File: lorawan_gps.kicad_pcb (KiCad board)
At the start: 2 copper layers, 75 x 20 mm, 59 parts, among them IC1 TPS61201, P1 BL_PAD, P10 CONN_01X01, P11 CONN_01X04, P2 SWD_DAT, P3 SWD_CLK, P4 SWD_3V3, P5 SWD_GND, P6 SWD_RST, P7 CONN_01X01, P8 CONN_01X01, P9 CONN_01X01, SW1 SW_PUSH, SW2 SW_PUSH, U1 SHT21, U2 MPU-9250, U3 RFM9xW, U4 SAMD21E17A, U5 MAX-M8, Y1 32.768kHz

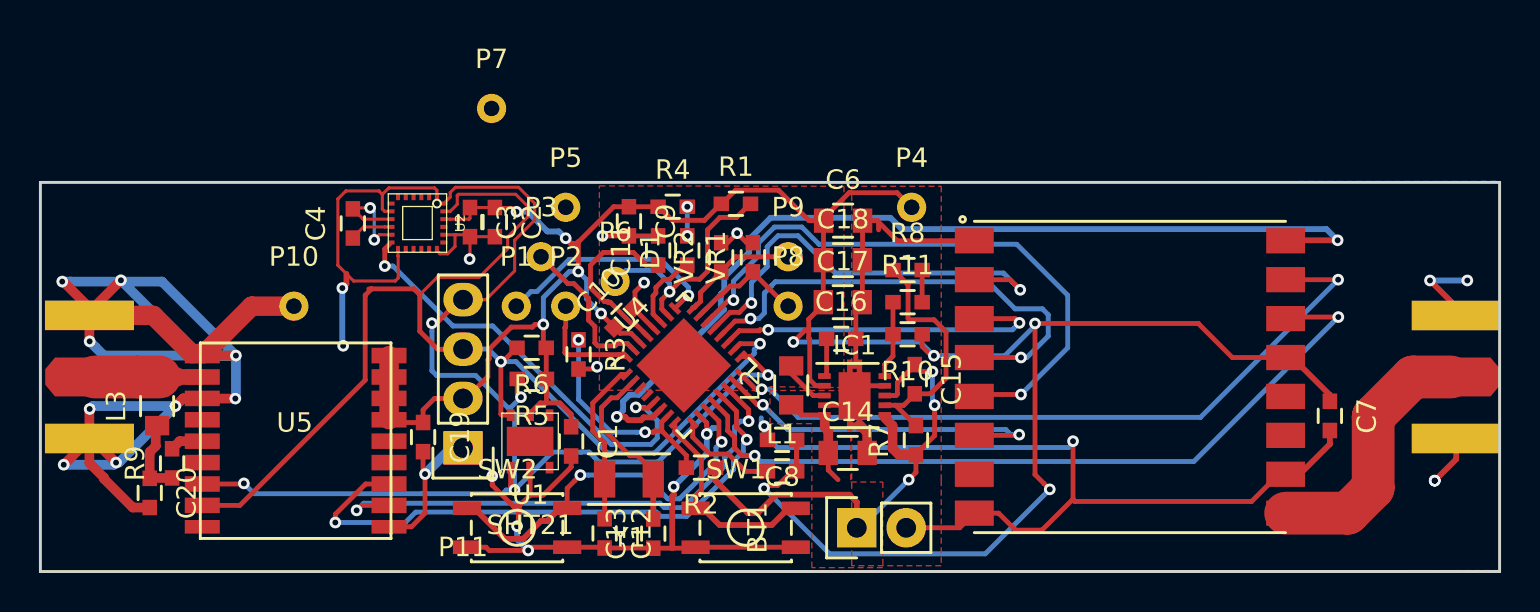
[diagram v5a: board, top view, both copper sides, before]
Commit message: moved battery input and fixed dodgy ground plane
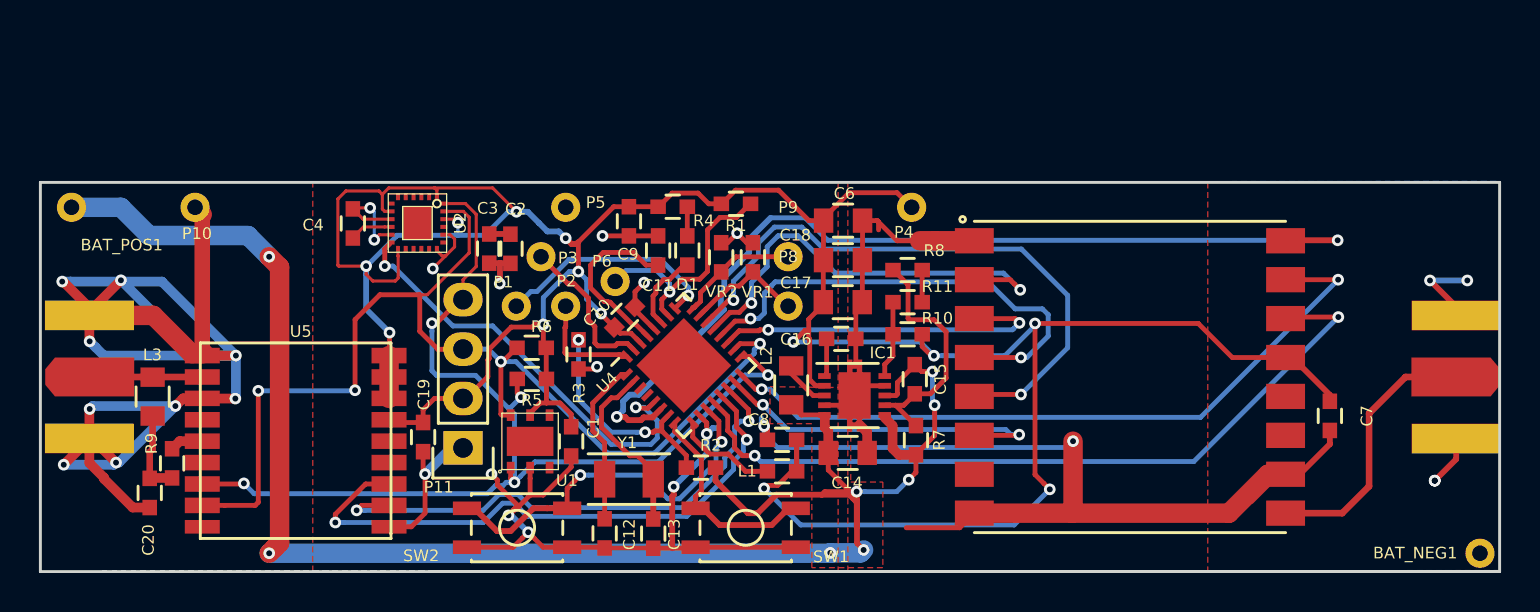
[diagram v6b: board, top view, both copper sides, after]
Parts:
- removed BT1: Battery, Pin_Headers:Pin_Header_Straight_1x02
- removed P7: CONN_01X01, Measurement_Points:Measurement_Point_Round-TH_Small
- added BAT_NEG1: CONN_01X01, Measurement_Points:Measurement_Point_Round-TH_Small, F.Cu at (174.0, 99.1)
- added BAT_POS1: CONN_01X01, Measurement_Points:Measurement_Point_Round-TH_Small, F.Cu at (101.6, 81.3)
- moved P10 7.18 mm to (108.0, 81.3)
- moved C3 1.68 mm to (123.1, 83.4)
- moved C2 1.59 mm to (124.2, 83.4)
- moved L3 0.54 mm to (105.8, 91.0)
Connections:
- U1 pad 3: Net-(U1-Pad3) -> (no net)
- U1 pad 4: Net-(U1-Pad4) -> (no net)
- U2 pad 14: Net-(U2-Pad14) -> (no net)
- U2 pad 15: Net-(U2-Pad15) -> (no net)
- U2 pad 16: Net-(U2-Pad16) -> (no net)
- U2 pad 17: Net-(U2-Pad17) -> (no net)
- U2 pad 19: Net-(U2-Pad19) -> (no net)
- U2 pad 2: Net-(U2-Pad2) -> (no net)
- U2 pad 21: Net-(U2-Pad21) -> (no net)
- U2 pad 3: Net-(U2-Pad3) -> (no net)
- U2 pad 4: Net-(U2-Pad4) -> (no net)
- U2 pad 5: Net-(U2-Pad5) -> (no net)
- U2 pad 6: Net-(U2-Pad6) -> (no net)
- U2 pad 7: Net-(U2-Pad7) -> (no net)
- U3 pad 11: Net-(U3-Pad11) -> (no net)
- U3 pad 12: Net-(U3-Pad12) -> (no net)
- U3 pad 7: Net-(U3-Pad7) -> (no net)
- U4 pad 3: Net-(U4-Pad3) -> (no net)
- U4 pad 4: Net-(U4-Pad4) -> (no net)
- U5 pad 13: Net-(U5-Pad13) -> (no net)
- U5 pad 15: Net-(U5-Pad15) -> (no net)
- U5 pad 18: Net-(U5-Pad18) -> (no net)
- U5 pad 4: Net-(U5-Pad4) -> (no net)
- U5 pad 5: Net-(U5-Pad5) -> (no net)
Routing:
- net /Battery/V_BAT: track 32.5 -> 98.2 mm, vias 3 -> 8
- net +3V3: track 154.5 -> 165.5 mm, vias 12 -> 13
- net /MCU/MPU_SDA: track 63.6 -> 56.4 mm
- net /MCU/MPU_SCL: track 62.2 -> 58.1 mm, vias 2 -> 4
- net GND: track 218.4 -> 222.2 mm, vias 28 -> 29
- net /GPS/GPS_FEEDER: track 8.70 -> 7.82 mm
- net Net-(D1-Pad2): track 1.50 -> 1.51 mm, vias 2 -> 0
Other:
- rule pad_to_mask_clearance: 0.2 -> 0

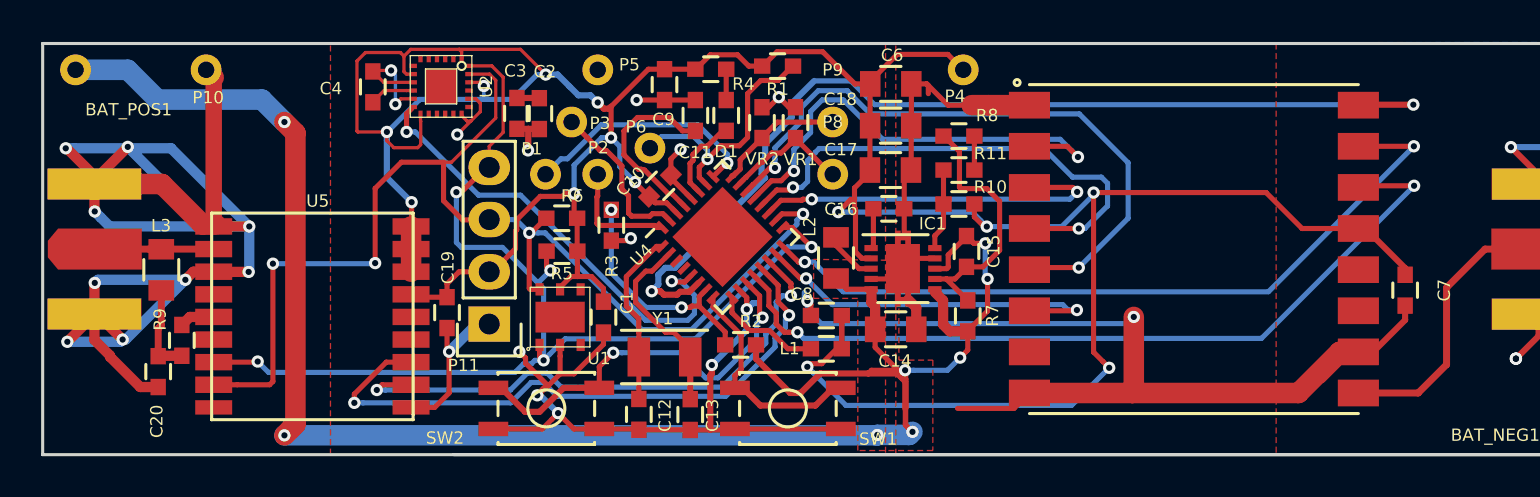
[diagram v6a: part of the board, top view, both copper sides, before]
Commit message: Changed L3 to 0603, L2 to 3x3, Fixed P8 silk and made gerbers
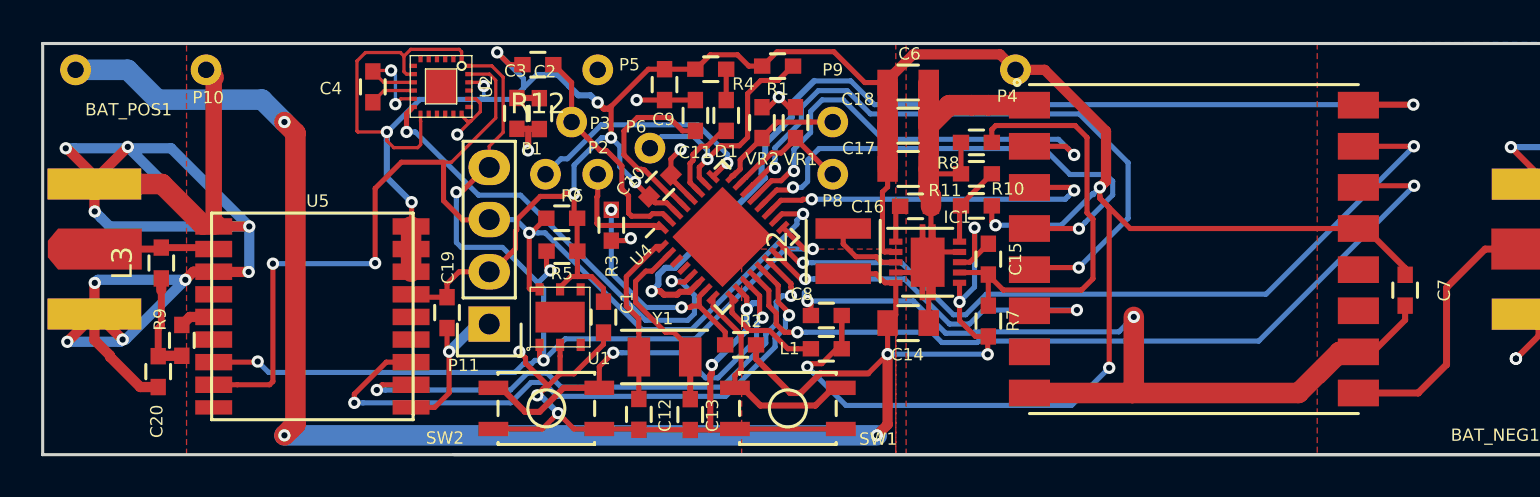
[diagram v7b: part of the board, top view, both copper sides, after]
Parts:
- added R12: 10k, Capacitors_SMD:C_0603, F.Cu at (124.1, 81.0)
- L2: footprint Capacitors_SMD:C_0805 -> Inductors_NEOSID:Neosid_Inductor_SMS-ME3015
- L3: footprint Capacitors_SMD:C_0805 -> Capacitors_SMD:C_0603
- moved P4 2.54 mm to (147.3, 81.3)
- moved C16 1.31 mm to (142.5, 87.9)
- moved IC1 1.24 mm to (143.1, 90.6)
- moved C15 1.13 mm to (146.0, 90.5)
- moved R7 1.03 mm to (146.0, 93.5)
- moved R8 0.90 mm to (145.4, 84.8), turned to 180 degrees
- moved R11 0.87 mm to (145.4, 86.3), turned to 180 degrees
- moved C17 0.86 mm to (142.1, 86.1)
- moved R10 0.86 mm to (145.4, 87.9)
- moved C18 0.85 mm to (142.1, 84.0)
- moved C6 0.85 mm to (142.1, 81.9)
- moved C14 0.68 mm to (142.1, 93.6)
- moved L2 0.48 mm to (138.9, 90.1)
- moved L3 0.33 mm to (105.8, 90.7)
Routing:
- net Net-(C15-Pad2): track 12.7 -> 21.2 mm
- net /Battery/V_BAT: track 98.2 -> 91.3 mm, vias 8 -> 7
- net Net-(P3-Pad1): track 7.99 -> 11.2 mm
- net GND: track 222.2 -> 223.9 mm
- net Net-(IC1-Pad3): track 2.57 -> 3.89 mm
- net /MCU/MPU_IN14: track 37.2 -> 38.2 mm
- net Net-(C20-Pad1): track 4.42 -> 5.00 mm
- net /MCU/MPU_D14: track 18.1 -> 18.7 mm
- net +3V3: track 165.5 -> 165.7 mm, vias 13 -> 12

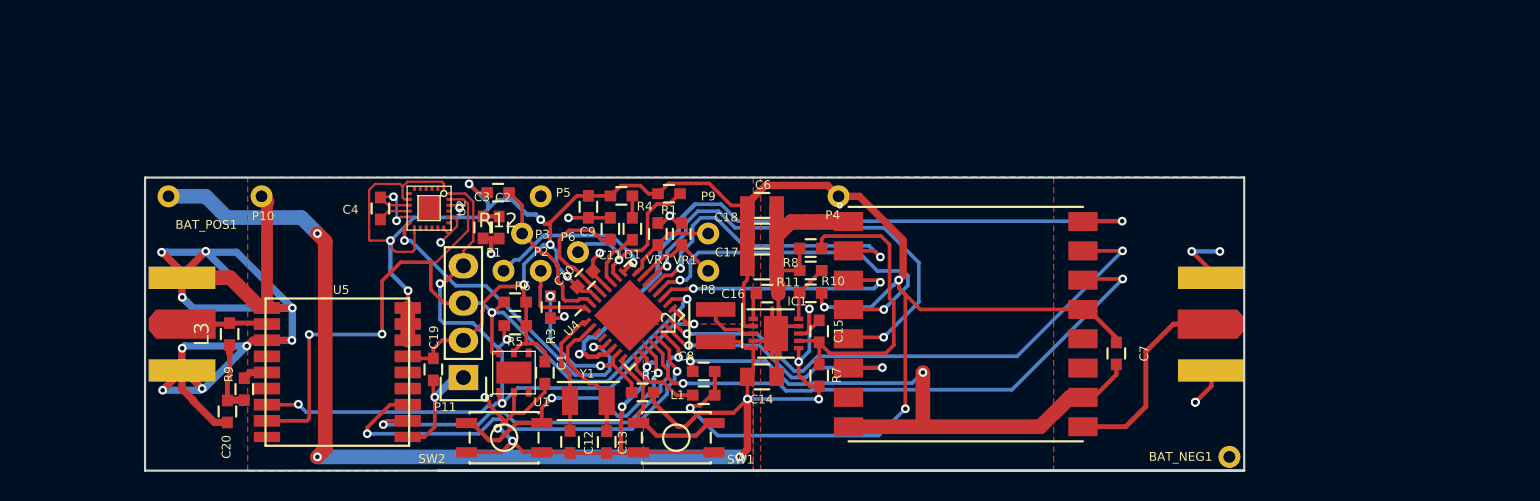
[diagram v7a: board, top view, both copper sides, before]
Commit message: Started changes after first round, micro usb connector, fixing footprint for accelerometer
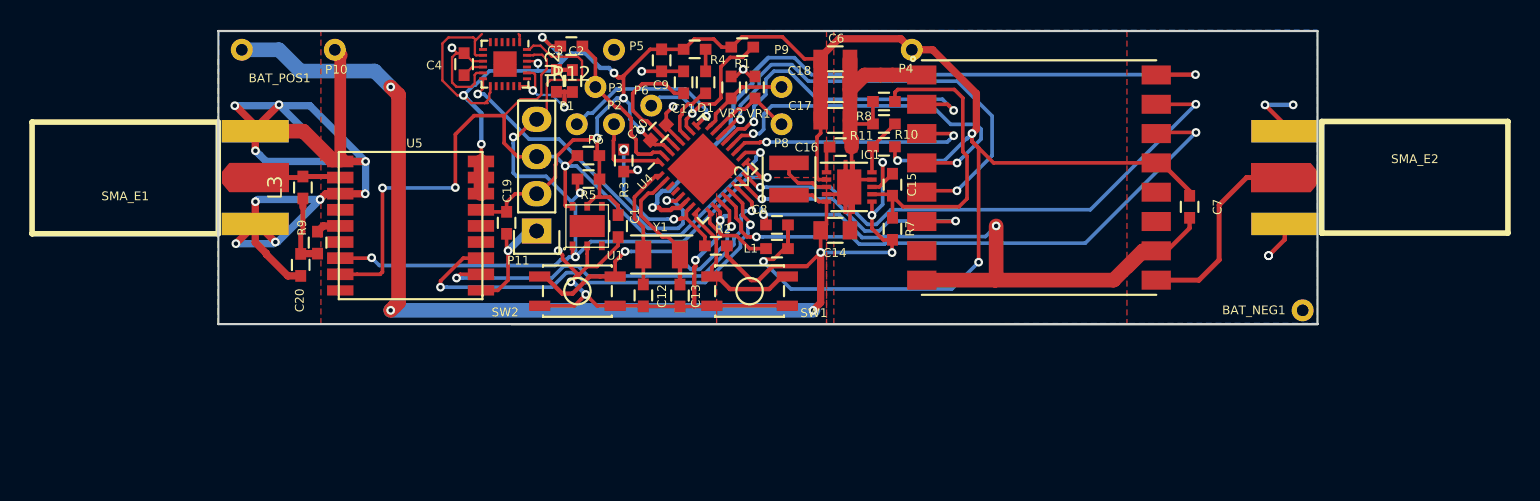
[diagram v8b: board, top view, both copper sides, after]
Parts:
- SMA_E1, SMA_E2: footprint SMA_EDGE:SMA_EDGE -> edgemount_sma:SMA_EDGE; moved to F.Cu
- U2: footprint mpu-9250:MPU-9250 -> Housings_DFN_QFN:QFN-24-1EP_3x3mm_Pitch0.4mm
- moved SMA_E2 13.5 mm to (186.6, 78.7)
- moved C4 11.4 mm to (121.8, 72.3)
- moved P1 11.2 mm to (129.5, 76.4)
- moved BAT_NEG1 11.2 mm to (179.0, 89.1)
- moved BAT_POS1 11.2 mm to (106.6, 71.3)
- moved C1 11.2 mm to (132.3, 83.3)
- moved C10 11.2 mm to (135.0, 76.9)
- moved C11 11.2 mm to (136.8, 73.5)
- moved C12 11.2 mm to (134.0, 88.0)
- moved C13 11.2 mm to (136.5, 88.0)
- moved C14 11.2 mm to (147.1, 83.6)
- moved C15 11.2 mm to (151.0, 80.5)
- moved C16 11.2 mm to (147.5, 77.9)
- moved C17 11.2 mm to (147.1, 76.1)
- moved C18 11.2 mm to (147.1, 74.0)
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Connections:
- U1 pad 3: (no net) -> Net-(U1-Pad3)
- U1 pad 4: (no net) -> Net-(U1-Pad4)
- U2 pad 14: (no net) -> Net-(U2-Pad14)
- U2 pad 15: (no net) -> Net-(U2-Pad15)
- U2 pad 16: (no net) -> Net-(U2-Pad16)
- U2 pad 17: (no net) -> Net-(U2-Pad17)
- U2 pad 19: (no net) -> Net-(U2-Pad19)
- U2 pad 2: (no net) -> Net-(U2-Pad2)
- U2 pad 21: (no net) -> Net-(U2-Pad21)
- U2 pad 3: (no net) -> Net-(U2-Pad3)
- U2 pad 4: (no net) -> Net-(U2-Pad4)
- U2 pad 5: (no net) -> Net-(U2-Pad5)
- U2 pad 6: (no net) -> Net-(U2-Pad6)
- U2 pad 7: (no net) -> Net-(U2-Pad7)
- U3 pad 11: (no net) -> Net-(U3-Pad11)
- U3 pad 12: (no net) -> Net-(U3-Pad12)
- U3 pad 7: (no net) -> Net-(U3-Pad7)
- U4 pad 3: (no net) -> Net-(U4-Pad3)
- U4 pad 4: (no net) -> Net-(U4-Pad4)
- U5 pad 13: (no net) -> Net-(U5-Pad13)
- U5 pad 15: (no net) -> Net-(U5-Pad15)
- U5 pad 18: (no net) -> Net-(U5-Pad18)
- U5 pad 4: (no net) -> Net-(U5-Pad4)
- U5 pad 5: (no net) -> Net-(U5-Pad5)
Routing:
- net GND: track 223.9 -> 228.3 mm, vias 29 -> 28
- net /MCU/MPU_SDA: track 56.5 -> 60.8 mm
- net +3V3: track 165.7 -> 162.6 mm
- net Net-(C4-Pad1): track 2.22 -> 1.52 mm
